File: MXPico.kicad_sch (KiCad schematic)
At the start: 27 parts, among them U1 Pico

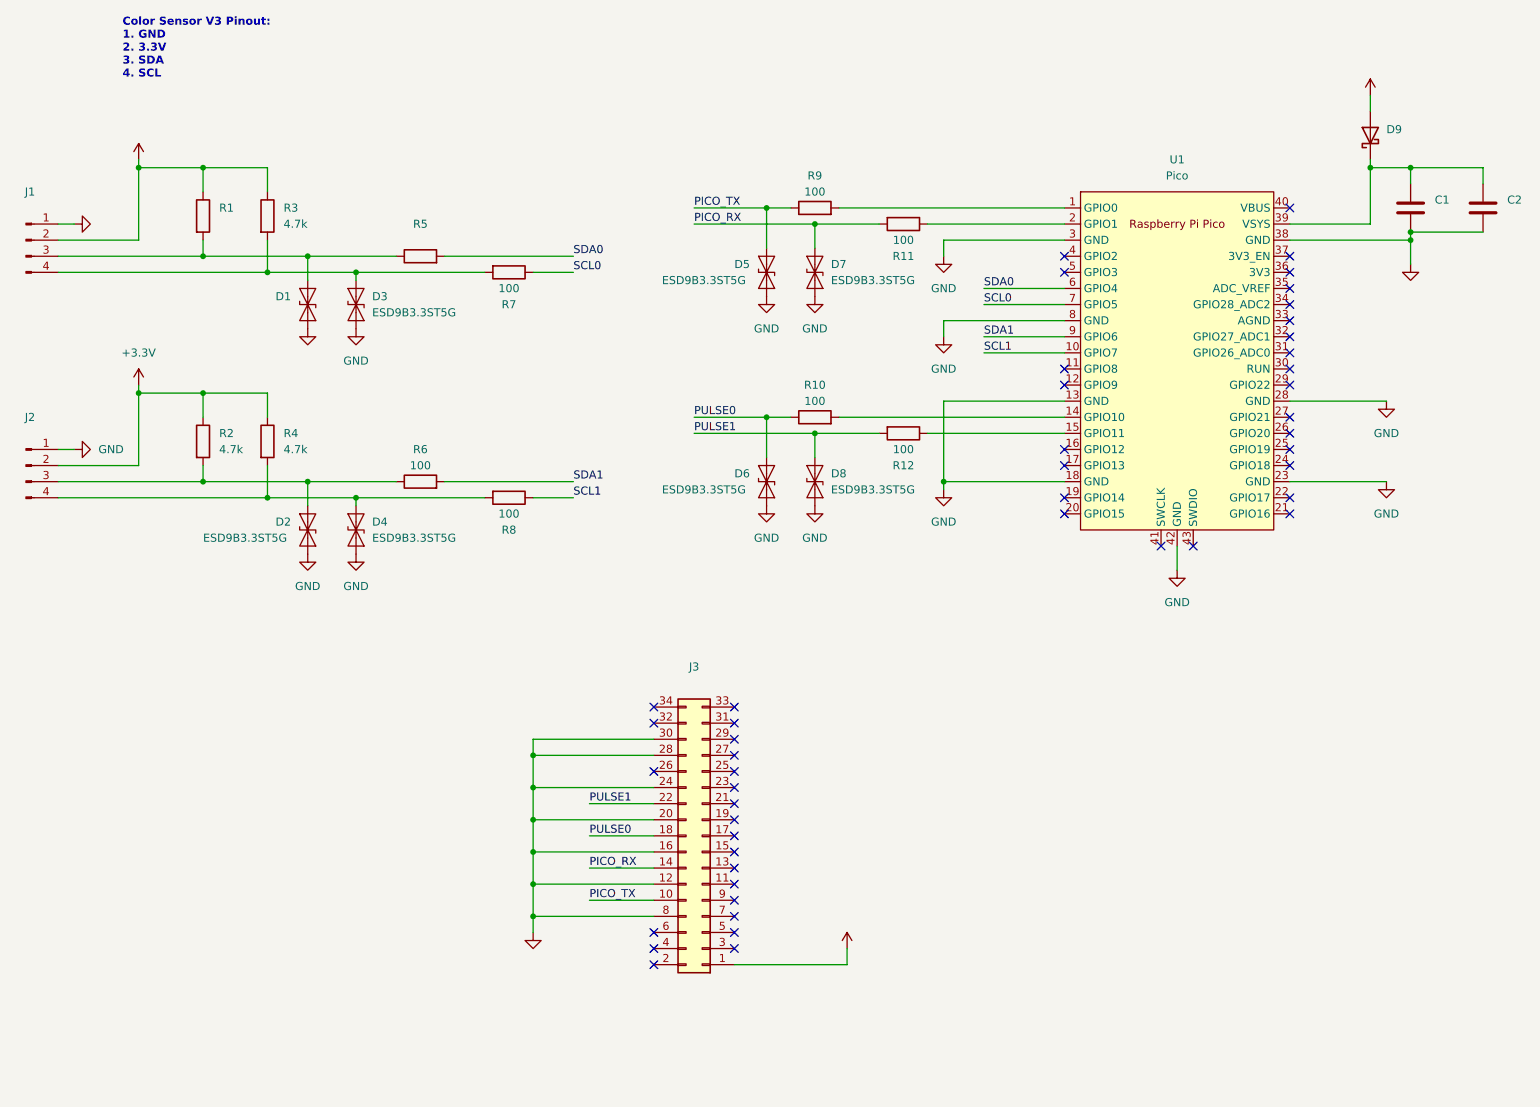
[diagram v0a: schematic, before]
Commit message: Adds +3.3V from MXP port and zeners
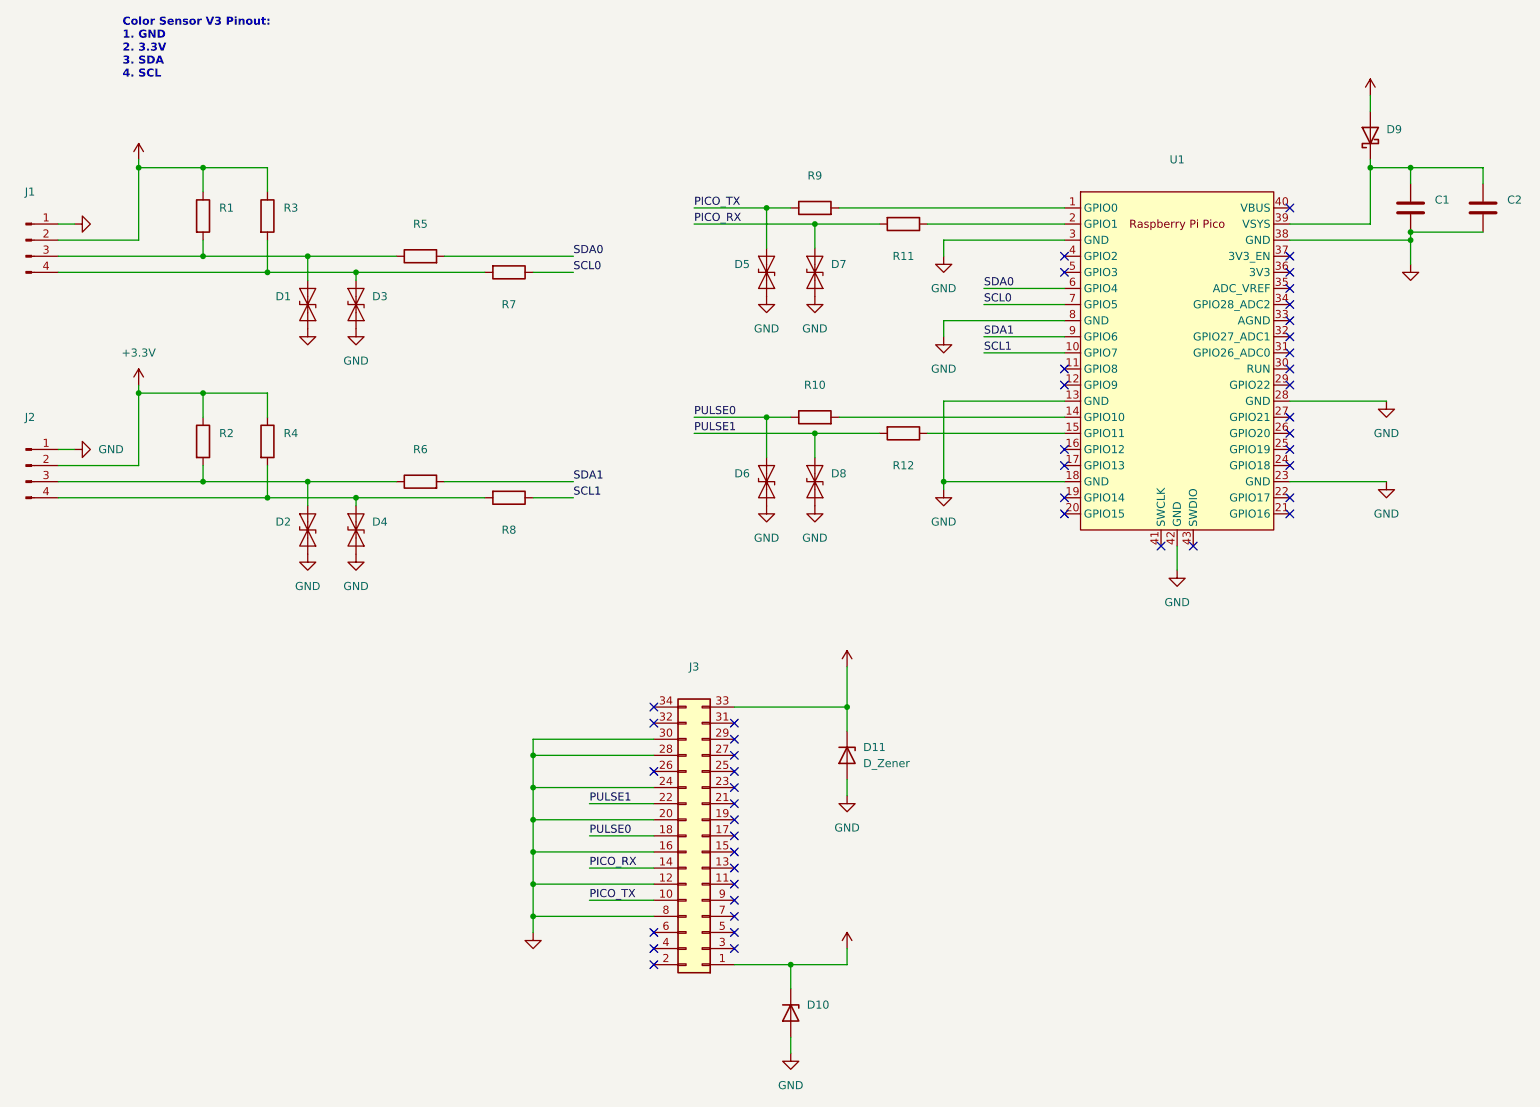
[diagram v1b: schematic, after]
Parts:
- added D10: (no value), symbol Device:D_Zener
- added D11: D_Zener, Diode_SMD:D_SOD-523, symbol Device:D_Zener
- D2, D3, D4, D5, D6, D7, D8: value ESD9B3.3ST5G -> (none); footprint Diode_SMD:D_SOD-923 -> (none)
- R10, R11, R12, R6, R7, R8, R9: value 100 -> (none)
- R2, R3, R4: value 4.7k -> (none)
- U1: value Pico -> (none); footprint RPi_Pico:RPi_Pico_SMD_TH -> (none)
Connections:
- net +3V3: now also J3.33 (Pin_33), D11.1 (K)
- net +5V: now also D10.1 (K)
- net GND: now also D10.2 (A), D11.2 (A)
- no-connect marks 48 -> 47

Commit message: Adds initial layout and fab files for E1
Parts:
- added C3, C4: 10uF, Resistor_SMD:R_0805_2012Metric, symbol Device:C
- added C5, C6: (no value), symbol Device:C
- added H1, H2: (no value), symbol Mechanical:MountingHole
- added J4: (no value), symbol Connector:Conn_01x04_Male
- added J5: (no value), Connector_PinHeader_2.54mm:PinHeader_1x04_P2.54mm_Vertical, symbol Connector:Conn_01x04_Male
- D11: value D_Zener -> (none); footprint Diode_SMD:D_SOD-523 -> (none)
- J3: Value2 (none) -> SFH11-PBPC-D17-ST-BK
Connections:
- net +3V3: now also C3.1, C4.1, J4.2 (Pin_2), J5.2 (Pin_2)
- net GND: now also C3.2, C4.2, C5.2, C6.2, J4.1 (Pin_1), J5.1 (Pin_1)
- net PICO_RX: now also C5.1
- net PICO_TX: now also C6.1
- net PULSE0: now also J3.31 (Pin_31); no longer J3.18 (Pin_18)
- net PULSE1: now also J3.29 (Pin_29); no longer J3.22 (Pin_22)
- net at D2.1 (A1), J2.3 (Pin_3), R2.2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: now also J5.4 (Pin_4)
- net at D4.1 (A1), J2.4 (Pin_4), R4.2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: now also J5.3 (Pin_3)
- net at D1.1 (A1), J1.3 (Pin_3), R1.2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: now also J4.4 (Pin_4)
- net at D3.1 (A1), J1.4 (Pin_4), R3.2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: now also J4.3 (Pin_3)
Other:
- note added: "RoboRIO Pinout: 1. GND 2. 3.3V 3. SCL 4. SDA"
